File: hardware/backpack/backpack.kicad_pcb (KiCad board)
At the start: 2 copper layers, 31.7 x 110 mm, 69 parts, among them J1 Conn_01x14_Socket, J2 Conn_02x06_Top_Bottom, J3 Conn_02x06_Top_Bottom, J4 MIDI_TRS_A, J5 MIDI_TRS_A, J6 CONN 2x5 P=2.54mm, J7 USB_C, J8 MICROMOD-2222, Q2 2N7002, Q3 2N7002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

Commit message: some rearranging
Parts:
- added J7: USB_C, cynthion:USB_C_Receptacle_HRO_TYPE-C-31-M-12, F.Cu at (2.40, 36.3)
- moved J1 62.9 mm to (10.7, 53.4), turned to 90 degrees
- moved REF** 49.3 mm to (14.9, 86.4), turned to 180 degrees
- moved J8 8.94 mm to (18.8, 66.6), turned to 0 degrees
- moved J7 2.00 mm to (2.45, 20.7)

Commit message: start power
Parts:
- added SW2: BTN_USER, cynthion:SW_Tactile_SPST_Angled_TC-1109DE-B-F, F.Cu at (3.00, 21.7)
- J1: moved to B.Cu
- moved R10 179.5 mm to (136.6, 31.7)
- moved R11 179.5 mm to (136.6, 33.7)
- moved R12 179.5 mm to (136.6, 35.7)
- moved R13 179.5 mm to (136.6, 37.7)
- moved R14 179.5 mm to (136.6, 39.7)
- moved R15 179.5 mm to (136.6, 41.7)
- moved R16 179.5 mm to (136.6, 43.7)
- moved U4 179.5 mm to (115.8, 54.6)
- moved D1 179.5 mm to (130.3, 51.6)
- moved Q2 179.5 mm to (125.1, 52.4)
- moved Q3 179.5 mm to (125.1, 57.0)
- moved C18 109.3 mm to (35.4, 50.6)
- moved C19 109.3 mm to (35.4, 52.6)
- moved C21 109.3 mm to (35.4, 56.5)
- moved R2 109.3 mm to (44.5, 52.6)
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- renumbered J7 to J8, SW3 to SW2

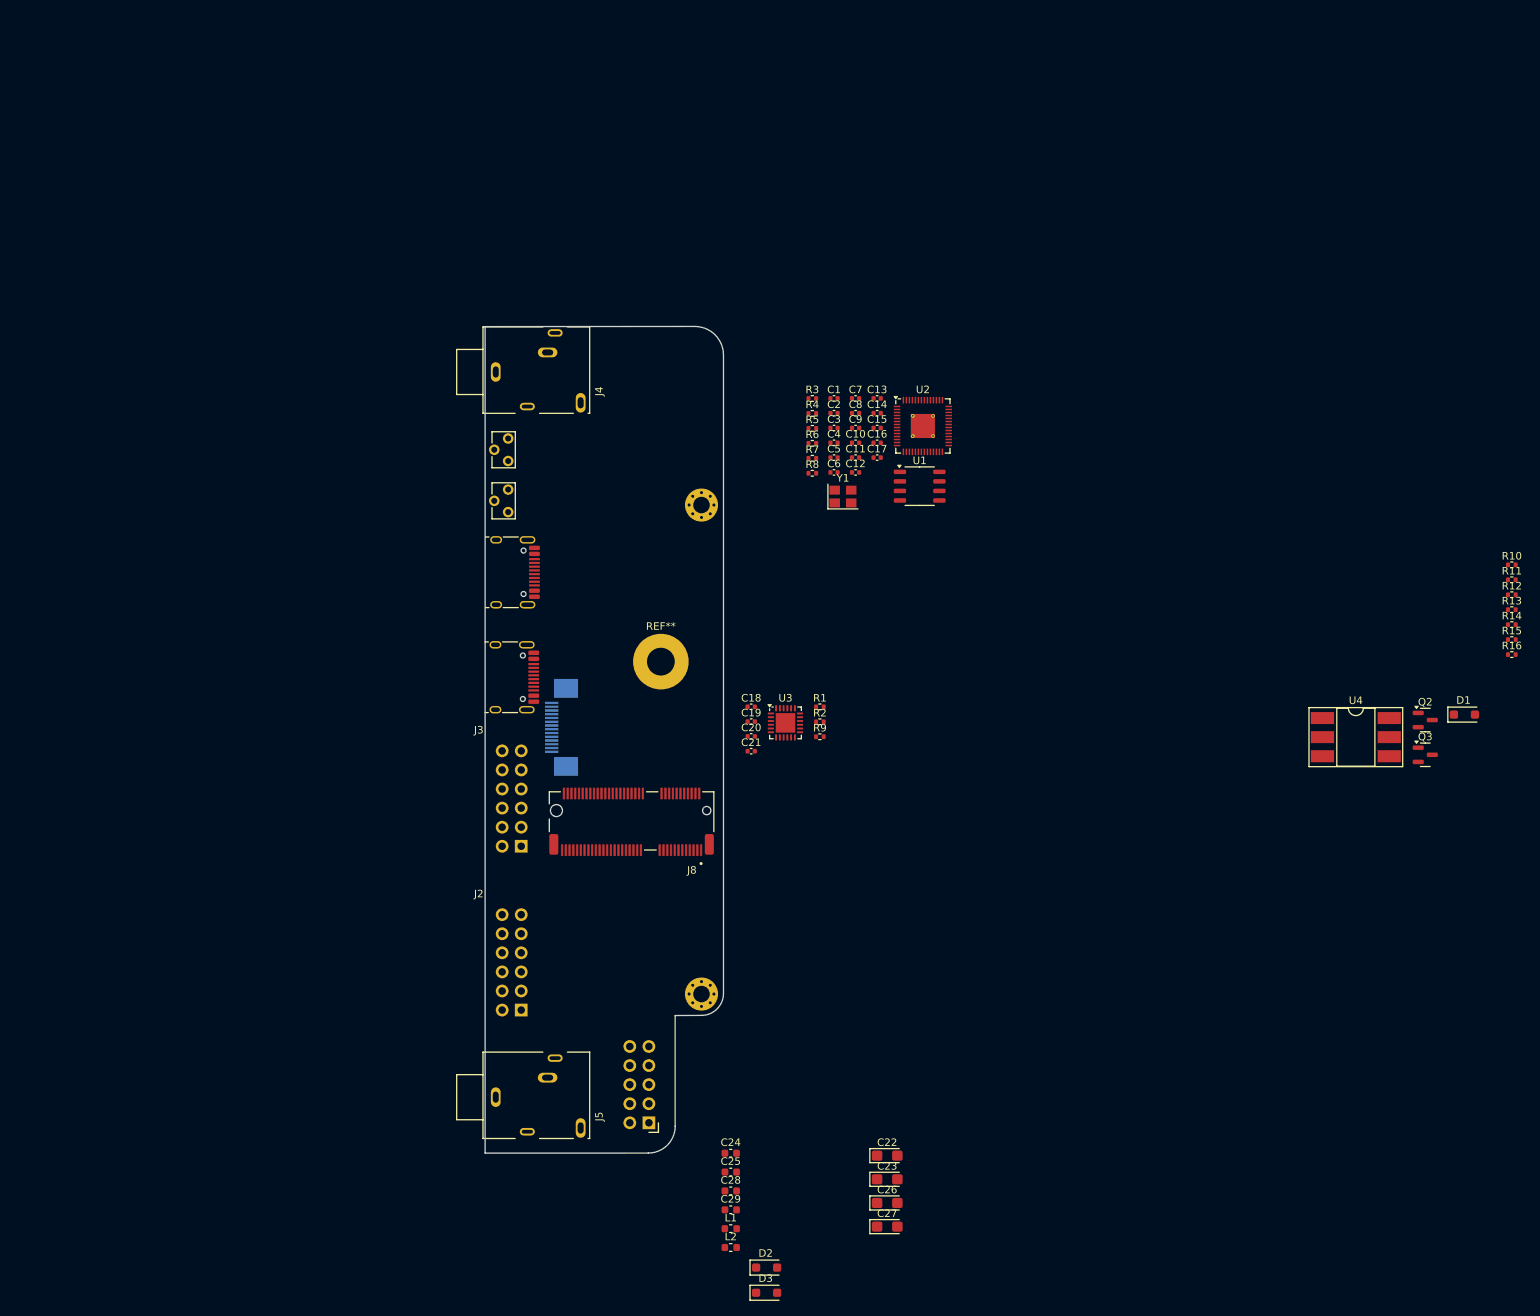
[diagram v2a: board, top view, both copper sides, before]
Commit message: parts and capture done sans most needing future pinswaps
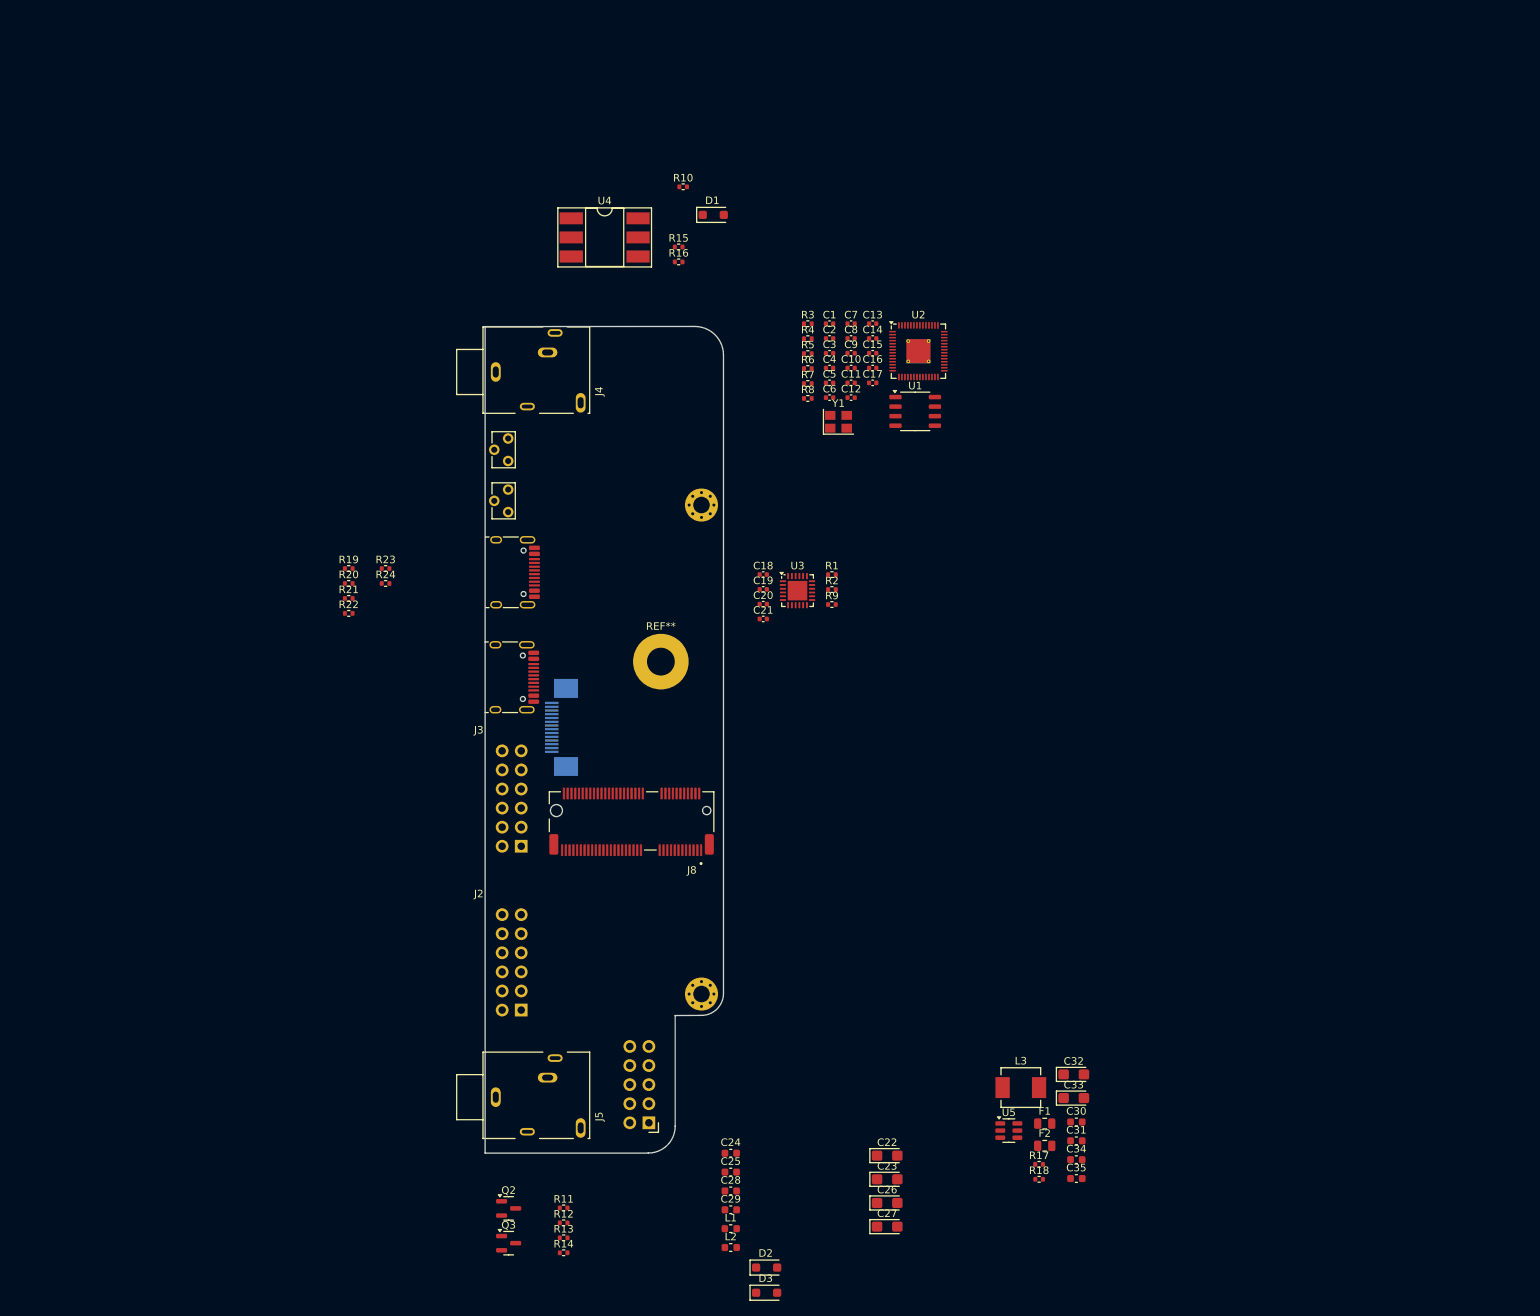
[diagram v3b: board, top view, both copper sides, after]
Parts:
- added C30: 100nF, Capacitor_SMD:C_0603_1608Metric, F.Cu at (78.6, 105.9)
- added C31: 100pF, Capacitor_SMD:C_0603_1608Metric, F.Cu at (78.6, 108.4)
- added C32: 22.0uF, Capacitor_Tantalum_SMD:CP_EIA-3216-10_Kemet-I, F.Cu at (78.3, 99.5)
- added C33: 22.0uF, Capacitor_Tantalum_SMD:CP_EIA-3216-10_Kemet-I, F.Cu at (78.3, 102.7)
- added C34: 100nF, Capacitor_SMD:C_0603_1608Metric, F.Cu at (78.6, 110.9)
- added C35: 100nF, Capacitor_SMD:C_0603_1608Metric, F.Cu at (78.6, 113.4)
- added F1: 15V 200mA, Fuse:Fuse_0805_2012Metric, F.Cu at (74.4, 106.1)
- added F2: 15V 200mA, Fuse:Fuse_0805_2012Metric, F.Cu at (74.4, 109.0)
- added L3: 6.8uH 2A, Inductor_SMD:L_Vishay_IHLP-2020, F.Cu at (71.2, 101.3)
- added R17: 182K, Resistor_SMD:R_0402_1005Metric, F.Cu at (73.7, 111.5)
- added R18: 62K, Resistor_SMD:R_0402_1005Metric, F.Cu at (73.7, 113.5)
- added R19: 5.1k, Resistor_SMD:R_0402_1005Metric, F.Cu at (-18.2, 32.2)
- added R20: 5.1k, Resistor_SMD:R_0402_1005Metric, F.Cu at (-18.2, 34.2)
- added R21: 5.1k, Resistor_SMD:R_0402_1005Metric, F.Cu at (-18.2, 36.2)
- added R22: 5.1k, Resistor_SMD:R_0402_1005Metric, F.Cu at (-18.2, 38.2)
- added R23: 10K, Resistor_SMD:R_0402_1005Metric, F.Cu at (-13.3, 32.2)
- added R24: 18K, Resistor_SMD:R_0402_1005Metric, F.Cu at (-13.3, 34.2)
- added U5: AP63200WU, Package_TO_SOT_SMD:TSOT-23-6, F.Cu at (69.6, 107.0)
- SW1: renamed from SW2; value BTN_USER -> ~
- SW2: value BTN_USER -> ~
- moved R11 151.4 mm to (10.4, 117.3)
- moved R12 151.4 mm to (10.4, 119.3)
- moved R13 151.4 mm to (10.4, 121.3)
- moved R14 151.4 mm to (10.4, 123.3)
- moved Q2 138.2 mm to (3.06, 117.4)
- moved Q3 138.2 mm to (3.06, 122.0)
- moved R15 122.6 mm to (25.7, -10.6)
- moved R16 122.6 mm to (25.7, -8.60)
- moved R10 121.2 mm to (26.3, -18.6)
- moved D1 120.1 mm to (30.3, -14.9)
- moved U4 120.1 mm to (15.8, -11.9)
- moved C18 17.7 mm to (37.0, 33.0)
- moved C19 17.7 mm to (37.0, 35.0)
- moved C21 17.7 mm to (37.0, 38.9)
- moved R2 17.7 mm to (46.1, 35.0)
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- renumbered J8 to J9
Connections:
- C21 pad 1: /usb/USB_VBUS_CONN -> /ULPI_USB_VBUS
- J1 pad 10: /pmod_audio/PMOD_3V3 -> +3V3
- J1 pad 11: /pmod_audio/PMOD_GNDA -> GND
- J1 pad 12: /pmod_audio/PMOD_P12V -> +12V
- J1 pad 14: /pmod_audio/PMOD_N12V -> -12V
- J1 pad 9: /pmod_audio/PMOD_GNDD -> GND
- J3 pad 1: (no net) -> unconnected-(J3-Pin_1-Pad1)
- J3 pad 10: (no net) -> unconnected-(J3-Pin_10-Pad10)
- J3 pad 11: (no net) -> GND
- J3 pad 12: (no net) -> +3V3
- J3 pad 2: (no net) -> unconnected-(J3-Pin_2-Pad2)
- J3 pad 3: (no net) -> unconnected-(J3-Pin_3-Pad3)
- J3 pad 4: (no net) -> unconnected-(J3-Pin_4-Pad4)
- J3 pad 5: (no net) -> GND
- J3 pad 6: (no net) -> +3V3
- J3 pad 7: (no net) -> unconnected-(J3-Pin_7-Pad7)
- J3 pad 8: (no net) -> unconnected-(J3-Pin_8-Pad8)
- J3 pad 9: (no net) -> unconnected-(J3-Pin_9-Pad9)
- J6 pad 1: Net-(D3-K) -> Net-(J6-Pin_1)
- J6 pad 10: Net-(D2-A) -> Net-(J6-Pin_10)
- J6 pad 2: Net-(D3-K) -> Net-(J6-Pin_1)
- J6 pad 9: Net-(D2-A) -> Net-(J6-Pin_10)
- J7 pad A1: (no net) -> GND
- J7 pad A12: (no net) -> GND
- J7 pad A4: (no net) -> /RP2040_USB_VBUS
- J7 pad A5: (no net) -> Net-(J7-CC1)
- J7 pad A6: (no net) -> /RP2040_USB_DP
- J7 pad A7: (no net) -> /RP2040_USB_DM
- J7 pad A8: (no net) -> unconnected-(J7-SBU1-PadA8)
- J7 pad A9: (no net) -> /RP2040_USB_VBUS
- J7 pad B1: (no net) -> GND
- J7 pad B12: (no net) -> GND
- J7 pad B4: (no net) -> /RP2040_USB_VBUS
- J7 pad B5: (no net) -> Net-(J7-CC2)
- J7 pad B6: (no net) -> /RP2040_USB_DP
- J7 pad B7: (no net) -> /RP2040_USB_DM
- J7 pad B8: (no net) -> unconnected-(J7-SBU2-PadB8)
- J7 pad B9: (no net) -> /RP2040_USB_VBUS
- J7 pad S1: (no net) -> GND
- J9 pad A1: (no net) -> GND
- J9 pad A12: (no net) -> GND
- J9 pad A4: (no net) -> /ULPI_USB_VBUS
- J9 pad A5: (no net) -> Net-(J9-CC1)
- J9 pad A6: (no net) -> /ULPI_USB_DP
- J9 pad A7: (no net) -> /ULPI_USB_DM
- J9 pad A8: (no net) -> unconnected-(J9-SBU1-PadA8)
- J9 pad A9: (no net) -> /ULPI_USB_VBUS
- J9 pad B1: (no net) -> GND
- J9 pad B12: (no net) -> GND
- J9 pad B4: (no net) -> /ULPI_USB_VBUS
- J9 pad B5: (no net) -> Net-(J9-CC2)
- J9 pad B6: (no net) -> /ULPI_USB_DP
- J9 pad B7: (no net) -> /ULPI_USB_DM
- J9 pad B8: (no net) -> unconnected-(J9-SBU2-PadB8)
- J9 pad B9: (no net) -> /ULPI_USB_VBUS
- J9 pad S1: (no net) -> GND
- R6 pad 1: /rp2040_jtag/USB_D- -> /RP2040_USB_DM
- R7 pad 1: /rp2040_jtag/USB_D+ -> /RP2040_USB_DP
- R9 pad 2: /usb/USB_VBUS_CONN -> /ULPI_USB_VBUS
- SW1 pad 1: (no net) -> unconnected-(SW1-Pad1)
- SW1 pad 2: (no net) -> unconnected-(SW1-Pad2)
- SW1 pad 3: (no net) -> unconnected-(SW1-SHIELD-Pad3)
- SW2 pad 1: (no net) -> GND
- SW2 pad 2: (no net) -> /rp2040_jtag/~{BOOTSEL}
- SW2 pad 3: (no net) -> unconnected-(SW2-SHIELD-Pad3)
- U2 pad 15: /rp2040_jtag/UART0_TX -> ECP5_A4
- U2 pad 16: /rp2040_jtag/UART0_RX -> ECP5_B4
- U2 pad 27: /rp2040_jtag/JTAG_TDI -> ECP5_R11_TDI
- U2 pad 28: /rp2040_jtag/JTAG_TDO -> ECP5_M10_TDO
- U2 pad 29: /rp2040_jtag/JTAG_TCK -> ECP5_T10_TCK
- U2 pad 30: /rp2040_jtag/JTAG_TMS -> ECP5_T11_TMS
- U2 pad 34: unconnected-(U2-GPIO22/SPI0_SCK/UART1_CTS/I2C1_SDA/PWM3_A/CLOCK_GPIN1/USB_VBUS_DET-Pad34) -> Net-(U2-GPIO22/SPI0_SCK/UART1_CTS/I2C1_SDA/PWM3_A/CLOCK_GPIN1/USB_VBUS_DET)
- U3 pad 13: /usb/USB_DP -> /ULPI_USB_DP
- U3 pad 14: /usb/USB_DM -> /ULPI_USB_DM
